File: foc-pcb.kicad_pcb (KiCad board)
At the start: 4 copper layers, 32 x 32 mm, 88 parts, among them IC1 THVD2450VDRCR, Q1 CSD18540Q5B, Q2 CSD18540Q5B, Q7 CSD18540Q5B, Q8 CSD18540Q5B, U1 UCC272847, U10 TPS63070, U12 C2901617, U17 DF52-4S-0.8H(21), U18 DF52-4S-0.8H(21)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

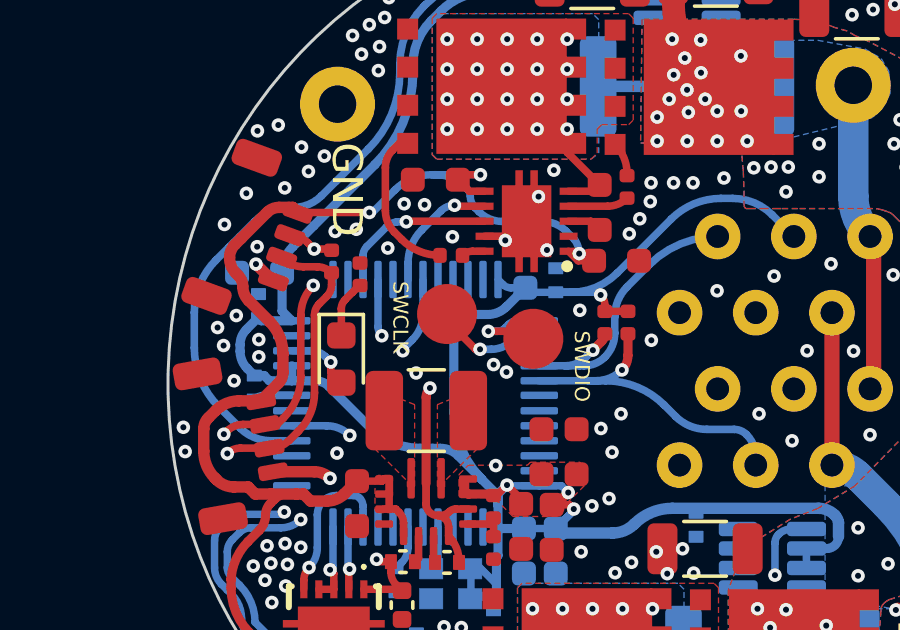
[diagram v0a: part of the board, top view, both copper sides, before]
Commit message: tweak pad location
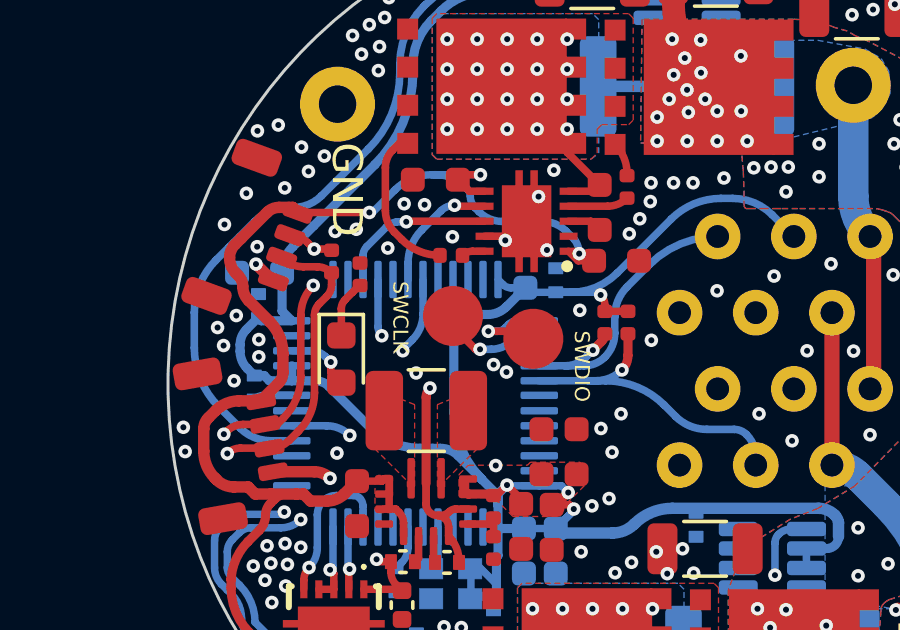
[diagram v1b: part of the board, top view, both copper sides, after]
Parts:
- moved U24 0.21 mm to (153.3, 131.7)
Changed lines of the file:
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@@
   )
   (footprint "foc-pcb-library:SMD_PROG_PAD" locked (layer "F.Cu")
-    (at 153.1 131.675)
+    (at 153.2961 131.7394)
     (property "Sheetfile" "STM32.kicad_sch")
     (property "Sheetname" "STM32")

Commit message: board clearance
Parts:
- moved C44 0.21 mm to (171.7, 127.3)
- moved C26 0.14 mm to (166.8, 121.7)
- moved U17 0.14 mm to (147.8, 129.5)
- moved C49 0.13 mm to (172.1, 127.0)
- moved C30 0.08 mm to (169.7, 124.3)
- moved U18 0.07 mm to (147.2, 135.7)
- moved C41 0.07 mm to (169.6, 124.2)
- turned C31 to 31 degrees
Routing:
- net /RS485/RS1_B: track 21.5 -> 22.1 mm
- net /STM32/TIM1_CH2N: track 29.8 -> 29.2 mm
